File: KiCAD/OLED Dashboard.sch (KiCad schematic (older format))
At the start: 0 parts

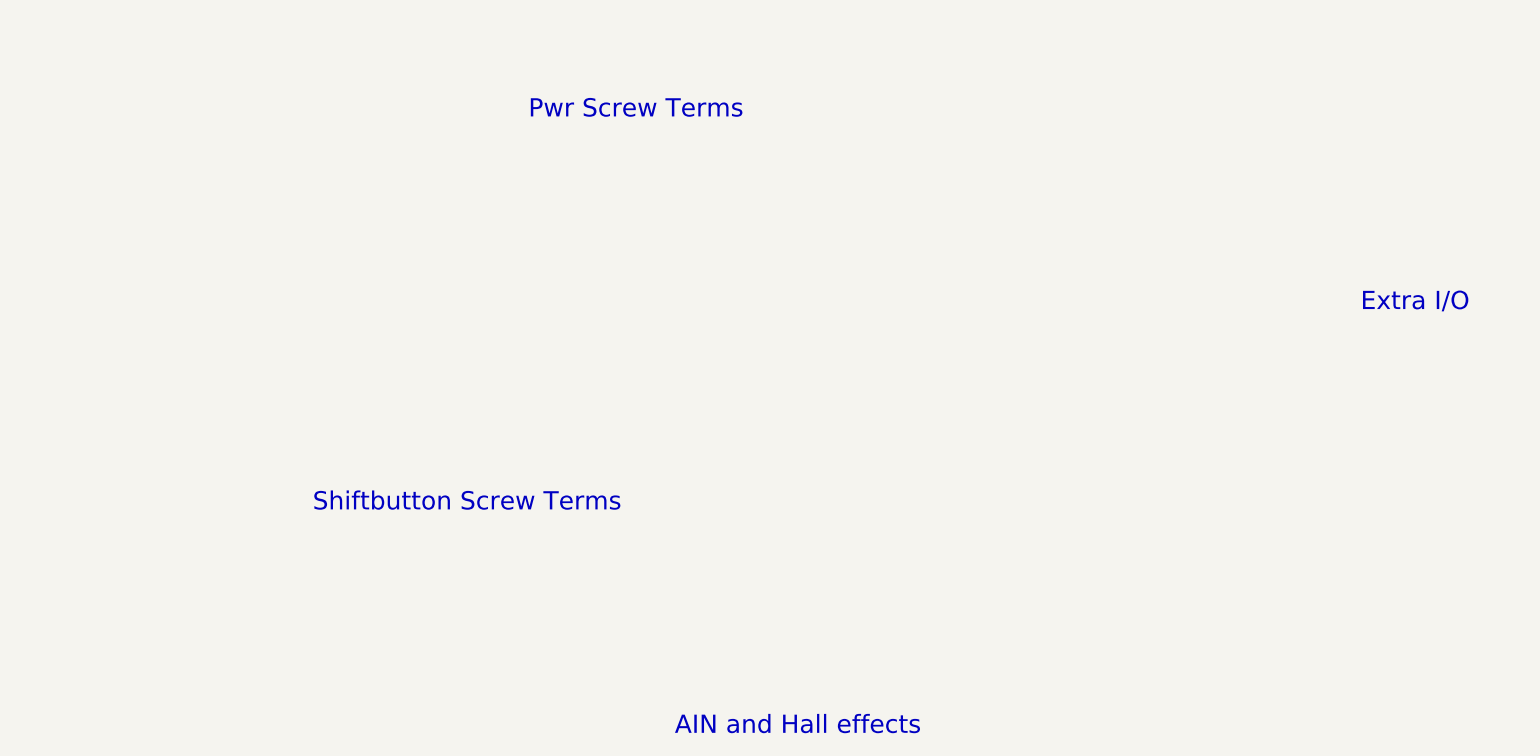
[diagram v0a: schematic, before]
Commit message: completed 5V buck schematic and setup
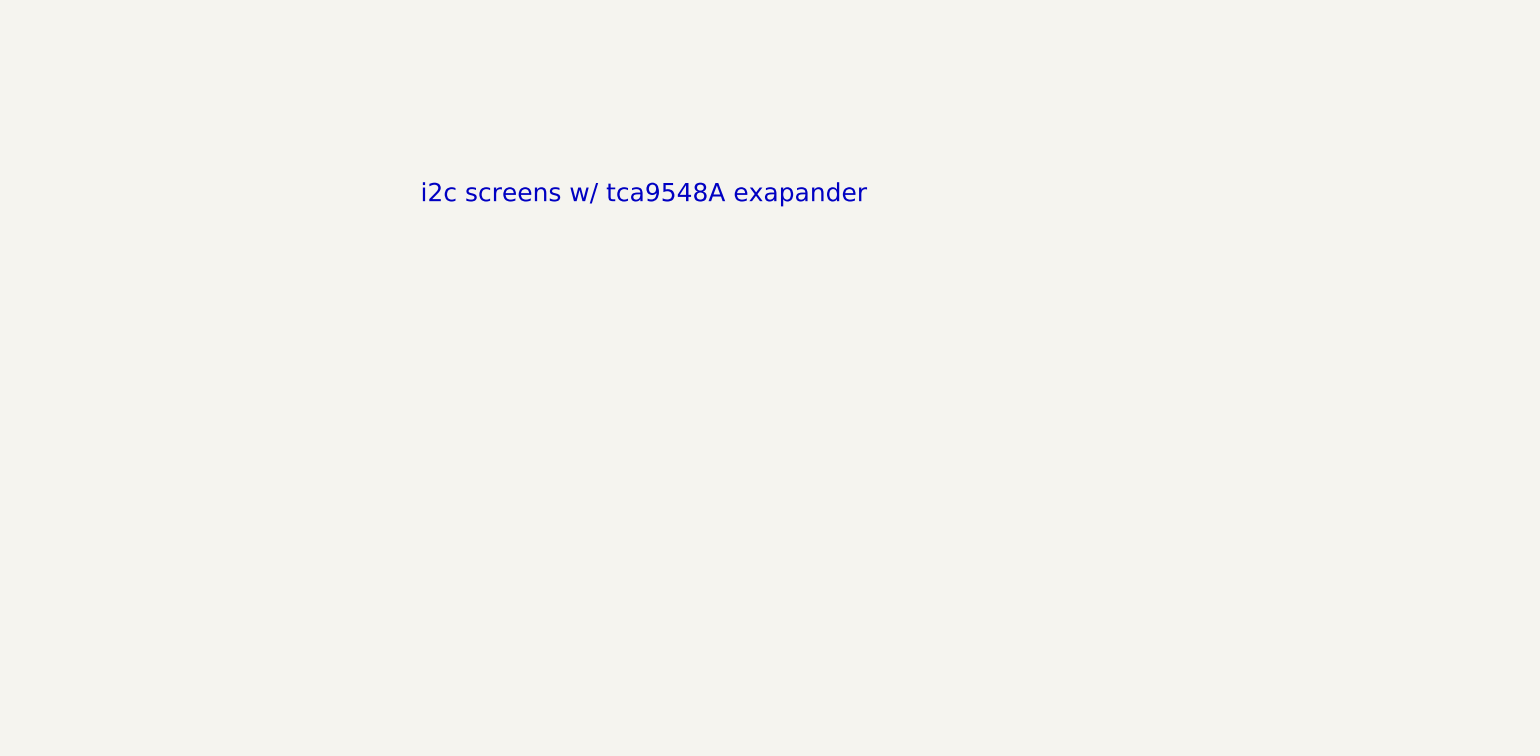
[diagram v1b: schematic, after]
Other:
- note added: "i2c screens w/ tca9548A exapander"
- note removed: "AIN and Hall effects"
- note removed: "Extra I/O"
- note removed: "Pwr Screw Terms\n"
- note removed: "Shiftbutton Screw Terms"
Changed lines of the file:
@@
 $Descr A4 11693 8268
 encoding utf-8
-Sheet 4 6
+Sheet 6 6
 Title ""
 Date ""
@@
 Comment4 ""
 $EndDescr
-Text Notes 3900 1300 0    118  ~ 0
-Pwr Screw Terms\n
-Text Notes 9300 2550 0    118  ~ 0
-Extra I/O
-Text Notes 4850 5300 0    118  ~ 0
-AIN and Hall effects
-Text Notes 2500 3850 0    118  ~ 0
-Shiftbutton Screw Terms
+Text Notes 3200 1850 0    118  ~ 0
+i2c screens w/ tca9548A exapander
 $EndSCHEMATC

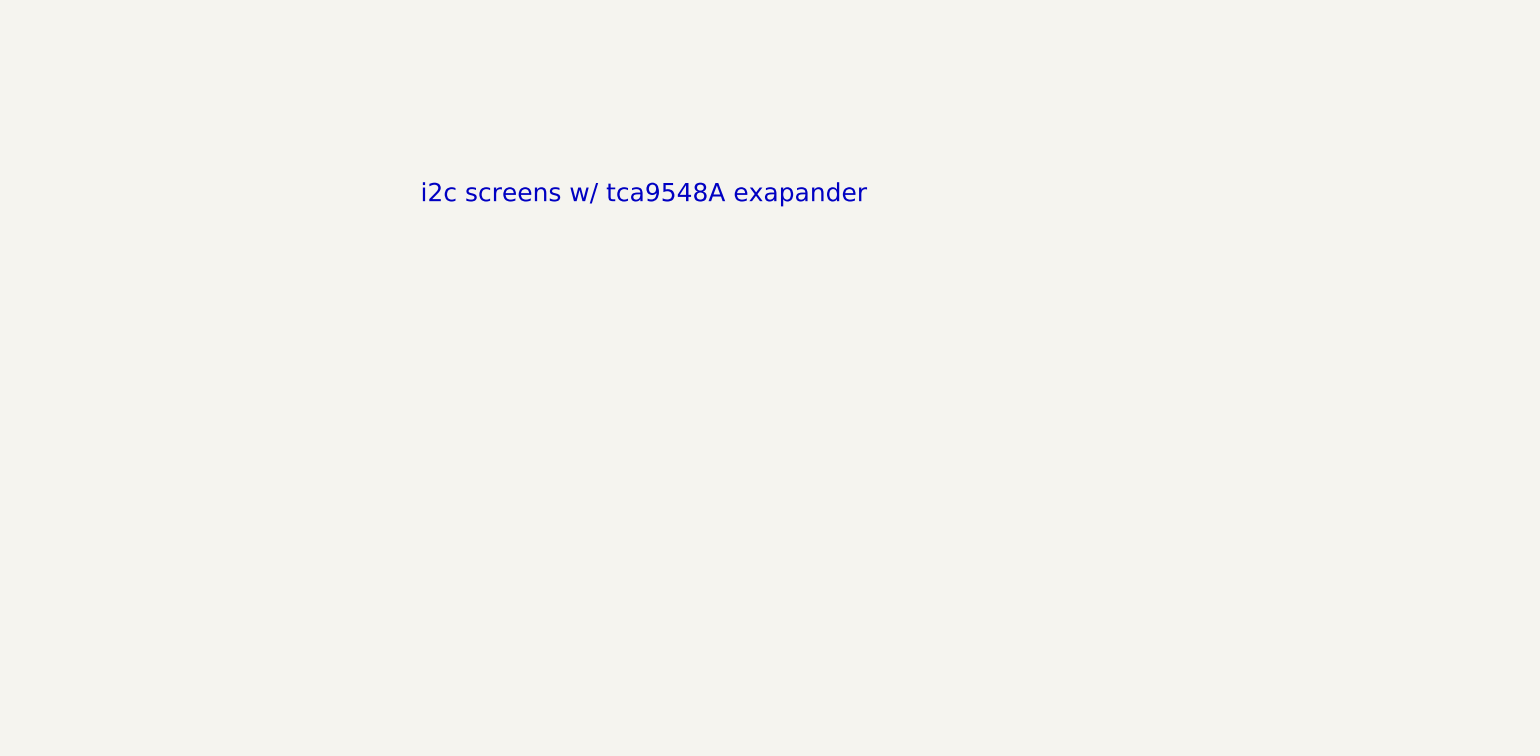
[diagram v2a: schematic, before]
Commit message: Schematic small fix
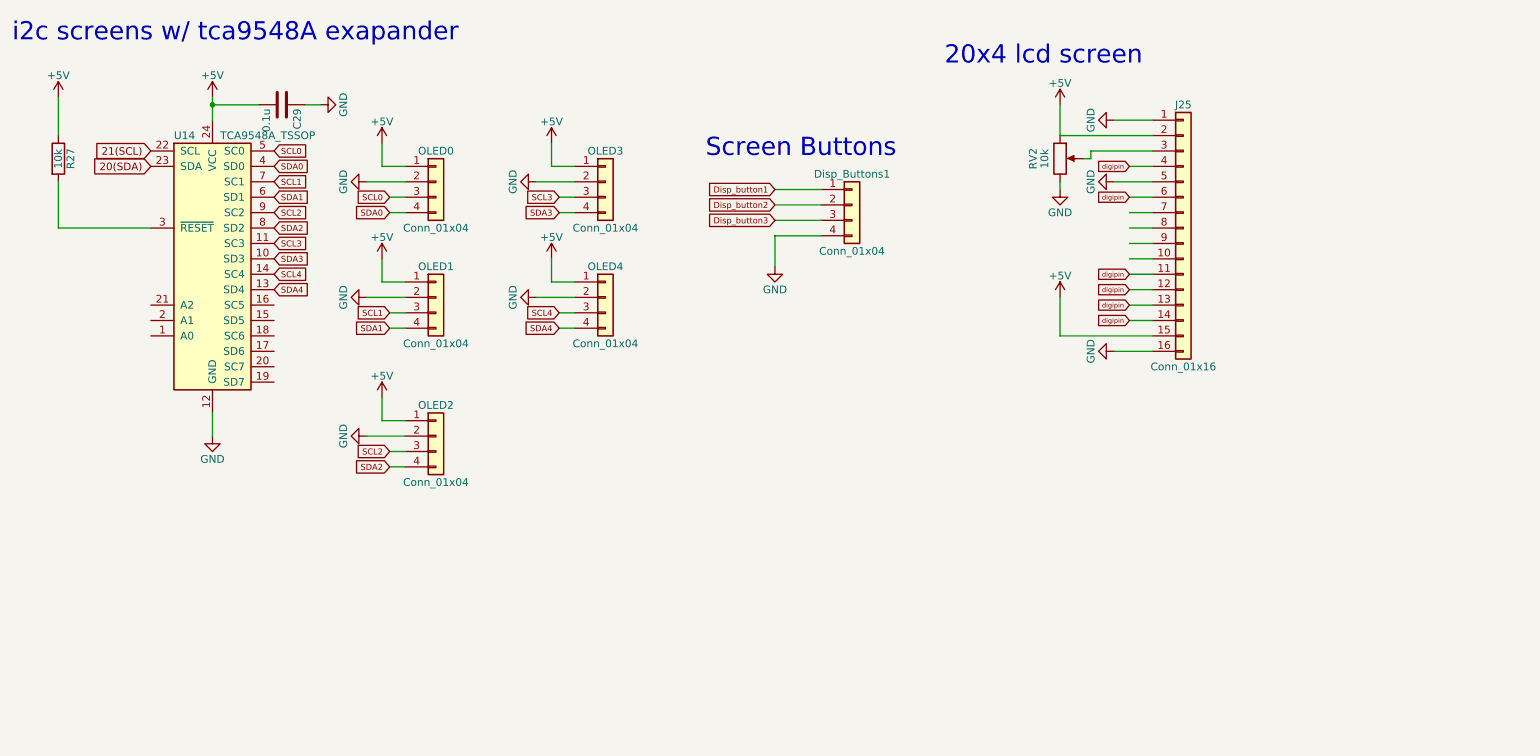
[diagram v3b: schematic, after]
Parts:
- added C29: 0.1u, Capacitors_SMD:C_0805, symbol C
- added Disp_Buttons1, OLED0, OLED1, OLED2, OLED3, OLED4: Conn_01x04, Pin_Headers:Pin_Header_Straight_1x04_Pitch2.54mm, symbol Conn_01x04
- added J25: Conn_01x16, Pin_Headers:Pin_Header_Straight_1x16_Pitch2.54mm, symbol Conn_01x16
- added R27: 10k, Resistors_SMD:R_0805, symbol R
- added RV2: 10k, Pin_Headers:Pin_Header_Straight_1x03_Pitch2.54mm, symbol POT
- added U14: TCA9548A_TSSOP, Housings_SSOP:TSSOP-24_4.4x7.8mm_Pitch0.65mm, symbol TCA9548A_TSSOP
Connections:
- net labels added: +5V, 20(SDA), 21(SCL), Disp_button1, Disp_button2, Disp_button3, GND, SCL0, SCL1, SCL2, SCL3, SCL4, SDA0, SDA1, SDA2, SDA3, SDA4, digipin
- wire segments 0 -> 58
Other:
- note added: "20x4 lcd screen\n"
- note added: "Screen Buttons"

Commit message: transfer for mechanical step
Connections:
- net labels added: 0(RX0), 1(TX0), 16(TX2), 17(RX2), 2(PWM), 3(PWM), 4(PWM), 6(PWM), A0
- net labels removed: digipin
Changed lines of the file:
@@
 Screen Buttons
 $Comp
-L GND #PWR0125
+L GND #PWR136
 U 1 1 5AEA6B6C
 P 5500 2250
-F 0 "#PWR0125" H 5500 2000 50  0001 C CNN
+F 0 "#PWR136" H 5500 2000 50  0001 C CNN
 F 1 "GND" H 5500 2100 50  0000 C CNN
 F 2 "" H 5500 2250 50  0001 C CNN
@@
 20(SDA)
 $Comp
-L +5V #PWR0126
+L +5V #PWR123
 U 1 1 5AED78CE
 P 1850 1150
-F 0 "#PWR0126" H 1850 1000 50  0001 C CNN
+F 0 "#PWR123" H 1850 1000 50  0001 C CNN
 F 1 "+5V" H 1850 1290 50  0000 C CNN
 F 2 "" H 1850 1150 50  0001 C CNN
@@
 	850  2000 850  1700
 $Comp
-L +5V #PWR0127
+L +5V #PWR122
 U 1 1 5AED7B9F
 P 850 1150
-F 0 "#PWR0127" H 850 1000 50  0001 C CNN
+F 0 "#PWR122" H 850 1000 50  0001 C CNN
 F 1 "+5V" H 850 1290 50  0000 C CNN
 F 2 "" H 850 1150 50  0001 C CNN
@@
 $EndComp
 $Comp
-L GND #PWR0128
+L GND #PWR125
 U 1 1 5AED7CB4
 P 2550 1200
-F 0 "#PWR0128" H 2550 950 50  0001 C CNN
+F 0 "#PWR125" H 2550 950 50  0001 C CNN
 F 1 "GND" H 2550 1050 50  0000 C CNN
 F 2 "" H 2550 1200 50  0001 C CNN
@@
 Connection ~ 1850 1200
 $Comp
-L GND #PWR0129
+L GND #PWR124
 U 1 1 5AED7DD2
 P 1850 3350
-F 0 "#PWR0129" H 1850 3100 50  0001 C CNN
+F 0 "#PWR124" H 1850 3100 50  0001 C CNN
 F 1 "GND" H 1850 3200 50  0000 C CNN
 F 2 "" H 1850 3350 50  0001 C CNN
@@
 $EndComp
 $Comp
-L +5V #PWR0130
+L +5V #PWR129
 U 1 1 5AED7E5F
 P 2950 1450
-F 0 "#PWR0130" H 2950 1300 50  0001 C CNN
+F 0 "#PWR129" H 2950 1300 50  0001 C CNN
 F 1 "+5V" H 2950 1590 50  0000 C CNN
 F 2 "" H 2950 1450 50  0001 C CNN
@@
 	2950 1600 2950 1450
 $Comp
-L GND #PWR0131
+L GND #PWR126
 U 1 1 5AED7E94
 P 2850 1700
-F 0 "#PWR0131" H 2850 1450 50  0001 C CNN
+F 0 "#PWR126" H 2850 1450 50  0001 C CNN
 F 1 "GND" H 2850 1550 50  0000 C CNN
 F 2 "" H 2850 1700 50  0001 C CNN
@@
 $EndComp
 $Comp
-L +5V #PWR0132
+L +5V #PWR130
 U 1 1 5AED8253
 P 2950 2200
-F 0 "#PWR0132" H 2950 2050 50  0001 C CNN
+F 0 "#PWR130" H 2950 2050 50  0001 C CNN
 F 1 "+5V" H 2950 2340 50  0000 C CNN
 F 2 "" H 2950 2200 50  0001 C CNN
@@
 	2950 2350 2950 2200
 $Comp
-L GND #PWR0133
+L GND #PWR127
 U 1 1 5AED825B
 P 2850 2450
-F 0 "#PWR0133" H 2850 2200 50  0001 C CNN
+F 0 "#PWR127" H 2850 2200 50  0001 C CNN
 F 1 "GND" H 2850 2300 50  0000 C CNN
 F 2 "" H 2850 2450 50  0001 C CNN
@@
 $EndComp
 $Comp
-L +5V #PWR0134
+L +5V #PWR134
 U 1 1 5AED8350
 P 4050 1450
-F 0 "#PWR0134" H 4050 1300 50  0001 C CNN
+F 0 "#PWR134" H 4050 1300 50  0001 C CNN
 F 1 "+5V" H 4050 1590 50  0000 C CNN
 F 2 "" H 4050 1450 50  0001 C CNN
@@
 	4050 1600 4050 1450
 $Comp
-L GND #PWR0135
+L GND #PWR132
 U 1 1 5AED8358
 P 3950 1700
-F 0 "#PWR0135" H 3950 1450 50  0001 C CNN
+F 0 "#PWR132" H 3950 1450 50  0001 C CNN
 F 1 "GND" H 3950 1550 50  0000 C CNN
 F 2 "" H 3950 1700 50  0001 C CNN
@@
 $EndComp
 $Comp
-L +5V #PWR0136
+L +5V #PWR135
 U 1 1 5AED8369
 P 4050 2200
-F 0 "#PWR0136" H 4050 2050 50  0001 C CNN
+F 0 "#PWR135" H 4050 2050 50  0001 C CNN
 F 1 "+5V" H 4050 2340 50  0000 C CNN
 F 2 "" H 4050 2200 50  0001 C CNN
@@
 	4050 2350 4050 2200
 $Comp
-L GND #PWR0137
+L GND #PWR133
 U 1 1 5AED8371
 P 3950 2450
-F 0 "#PWR0137" H 3950 2200 50  0001 C CNN
+F 0 "#PWR133" H 3950 2200 50  0001 C CNN
 F 1 "GND" H 3950 2300 50  0000 C CNN
 F 2 "" H 3950 2450 50  0001 C CNN
@@
 $EndComp
 $Comp
-L +5V #PWR0138
+L +5V #PWR131
 U 1 1 5AED83B1
 P 2950 3100
-F 0 "#PWR0138" H 2950 2950 50  0001 C CNN
+F 0 "#PWR131" H 2950 2950 50  0001 C CNN
 F 1 "+5V" H 2950 3240 50  0000 C CNN
 F 2 "" H 2950 3100 50  0001 C CNN
@@
 	2950 3250 2950 3100
 $Comp
-L GND #PWR0139
+L GND #PWR128
 U 1 1 5AED83B9
 P 2850 3350
-F 0 "#PWR0139" H 2850 3100 50  0001 C CNN
+F 0 "#PWR128" H 2850 3100 50  0001 C CNN
 F 1 "GND" H 2850 3200 50  0000 C CNN
 F 2 "" H 2850 3350 50  0001 C CNN
@@
 	7700 2800 7950 2800
 $Comp
-L GND #PWR0140
+L GND #PWR140
 U 1 1 5AED9E88
 P 7700 1300
-F 0 "#PWR0140" H 7700 1050 50  0001 C CNN
+F 0 "#PWR140" H 7700 1050 50  0001 C CNN
 F 1 "GND" H 7700 1150 50  0000 C CNN
 F 2 "" H 7700 1300 50  0001 C CNN
@@
 $EndComp
 $Comp
-L +5V #PWR0141
+L +5V #PWR137
 U 1 1 5AED9EB1
 P 7350 1200
-F 0 "#PWR0141" H 7350 1050 50  0001 C CNN
+F 0 "#PWR137" H 7350 1050 50  0001 C CNN
 F 1 "+5V" H 7350 1340 50  0000 C CNN
 F 2 "" H 7350 1200 50  0001 C CNN
@@
 	7550 1550 7500 1550
 $Comp
-L GND #PWR0142
+L GND #PWR138
 U 1 1 5AEDA6FB
 P 7350 1750
-F 0 "#PWR0142" H 7350 1500 50  0001 C CNN
+F 0 "#PWR138" H 7350 1500 50  0001 C CNN
 F 1 "GND" H 7350 1600 50  0000 C CNN
 F 2 "" H 7350 1750 50  0001 C CNN
@@
 	7350 1750 7350 1700
 $Comp
-L GND #PWR0143
+L GND #PWR142
 U 1 1 5AEDAAF5
 P 7700 2800
-F 0 "#PWR0143" H 7700 2550 50  0001 C CNN
+F 0 "#PWR142" H 7700 2550 50  0001 C CNN
 F 1 "GND" H 7700 2650 50  0000 C CNN
 F 2 "" H 7700 2800 50  0001 C CNN
@@
 $EndComp
 $Comp
-L +5V #PWR0144
+L +5V #PWR139
 U 1 1 5AEDAAFB
 P 7350 2450
-F 0 "#PWR0144" H 7350 2300 50  0001 C CNN
+F 0 "#PWR139" H 7350 2300 50  0001 C CNN
 F 1 "+5V" H 7350 2590 50  0000 C CNN
 F 2 "" H 7350 2450 50  0001 C CNN
@@
 	7350 2450 7350 2700
 Text GLabel 7800 1600 0    31   Input ~ 0
-digipin
-$Comp
-L GND #PWR0145
+3(PWM)
+$Comp
+L GND #PWR141
 U 1 1 5AEDABC8
 P 7700 1700
-F 0 "#PWR0145" H 7700 1450 50  0001 C CNN
+F 0 "#PWR141" H 7700 1450 50  0001 C CNN
 F 1 "GND" H 7700 1550 50  0000 C CNN
 F 2 "" H 7700 1700 50  0001 C CNN
@@
 $EndComp
 Text GLabel 7800 1800 0    31   Input ~ 0
-digipin
+2(PWM)
 Text GLabel 7800 2600 0    31   Input ~ 0
-digipin
+A0
 Text GLabel 7800 2500 0    31   Input ~ 0
-digipin
+4(PWM)
 Text GLabel 7800 2400 0    31   Input ~ 0
-digipin
+0(RX0)
 Text GLabel 7800 2300 0    31   Input ~ 0
-digipin
+1(TX0)
+Text GLabel 1450 2700 0    39   Input ~ 0
+17(RX2)
+Text GLabel 1450 2600 0    39   Input ~ 0
+16(TX2)
+Text GLabel 1450 2500 0    39   Input ~ 0
+6(PWM)
 $EndSCHEMATC
